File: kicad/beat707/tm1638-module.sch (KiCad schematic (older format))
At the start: 103 parts, among them SW10 SW_Push, SW11 SW_Push, SW12 SW_Push, SW13 SW_Push, SW14 SW_Push, SW15 SW_Push, SW16 SW_Push, SW17 SW_Push, SW18 SW_Push, SW19 SW_Push, SW20 SW_Push, SW21 SW_Push, SW22 SW_Push, SW23 SW_Push, SW24 SW_Push, SW25 SW_Push, SW26 SW_Push, SW27 SW_Push, SW28 SW_Push, SW5 SW_Push, SW6 SW_Push, SW7 SW_Push, SW8 SW_Push, SW9 SW_Push, U6 TM1638, U7 CA56-12EWA, U8 CA56-12EWA

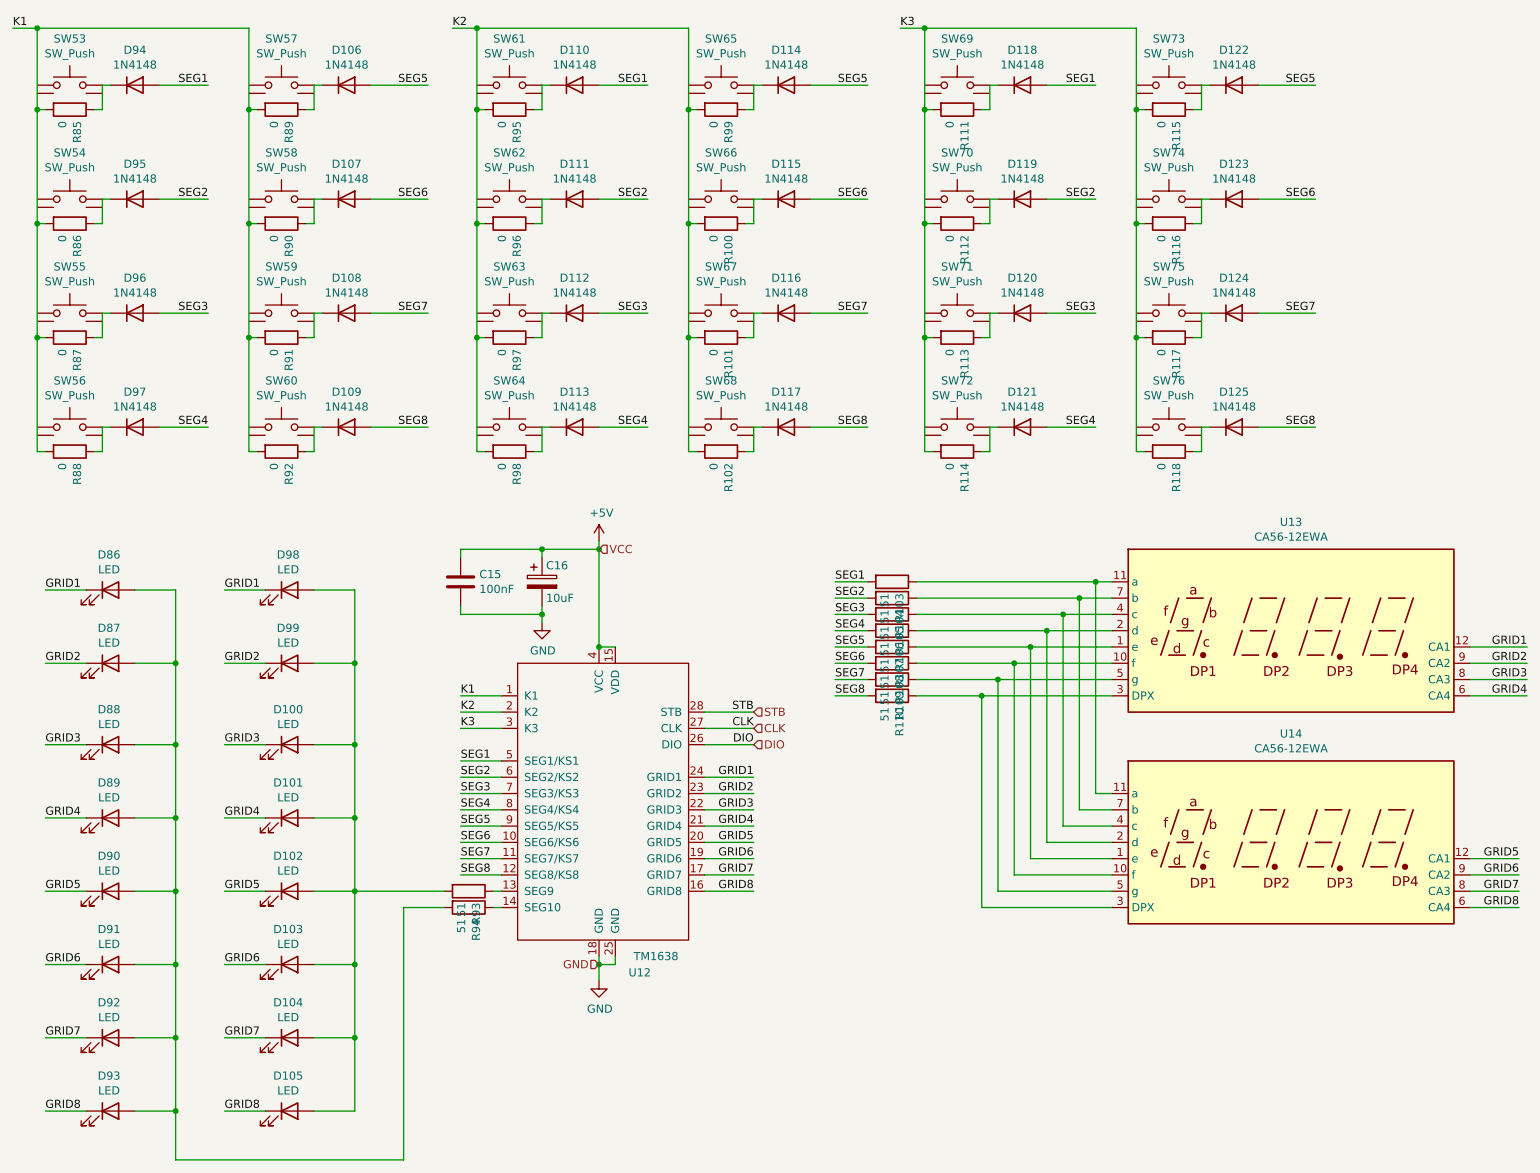
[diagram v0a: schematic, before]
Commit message: brain board added, bufixes and final board synchronized with schematic
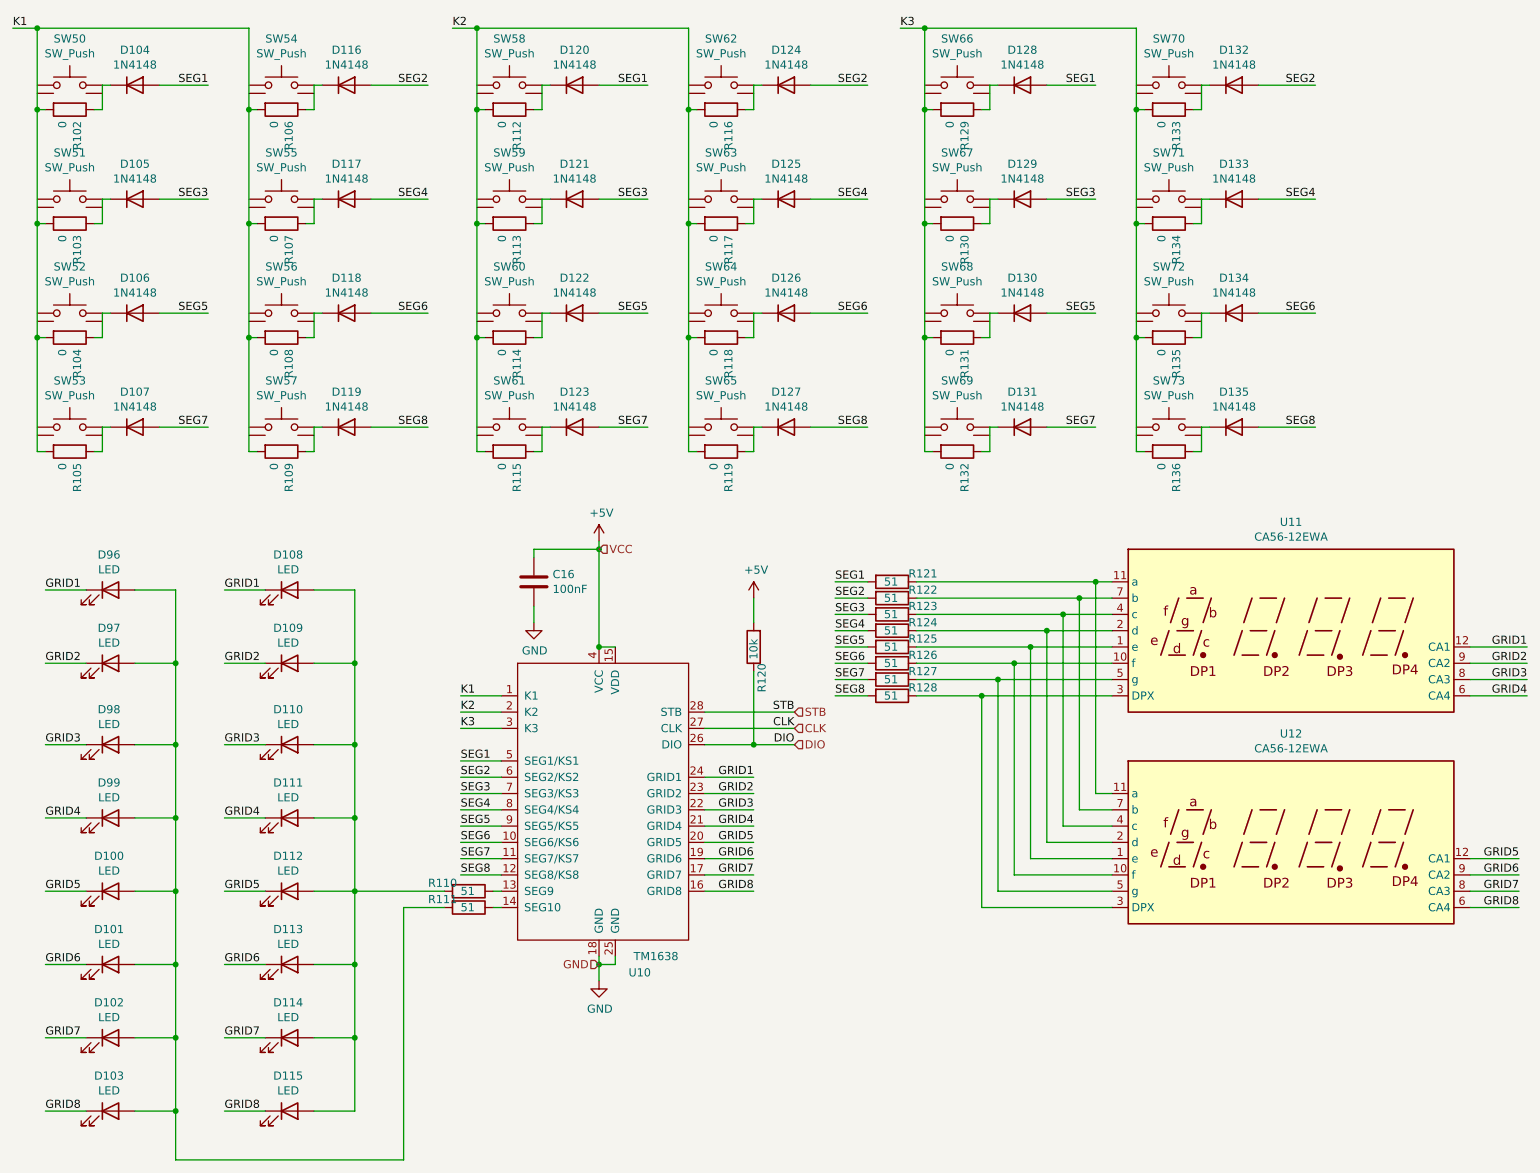
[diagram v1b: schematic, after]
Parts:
- removed C12: 10uF, Capacitor_THT:CP_Radial_D6.3mm_P2.50mm, symbol Device:CP
- added R85: 10k, Resistor_THT:R_Axial_DIN0207_L6.3mm_D2.5mm_P10.16mm_Horizontal, symbol Device:R
- R100: renamed from R83; footprint Resistor_THT:R_Axial_DIN0207_L6.3mm_D2.5mm_P7.62mm_Horizontal -> Resistor_THT:R_Axial_DIN0207_L6.3mm_D2.5mm_P10.16mm_Horizontal
- R101: renamed from R84; footprint Resistor_THT:R_Axial_DIN0207_L6.3mm_D2.5mm_P7.62mm_Horizontal -> Resistor_THT:R_Axial_DIN0207_L6.3mm_D2.5mm_P10.16mm_Horizontal
- R67: renamed from R51; footprint Resistor_THT:R_Axial_DIN0207_L6.3mm_D2.5mm_P7.62mm_Horizontal -> Resistor_THT:R_Axial_DIN0207_L6.3mm_D2.5mm_P10.16mm_Horizontal
- R68: renamed from R52; footprint Resistor_THT:R_Axial_DIN0207_L6.3mm_D2.5mm_P7.62mm_Horizontal -> Resistor_THT:R_Axial_DIN0207_L6.3mm_D2.5mm_P10.16mm_Horizontal
- R69: renamed from R53; footprint Resistor_THT:R_Axial_DIN0207_L6.3mm_D2.5mm_P7.62mm_Horizontal -> Resistor_THT:R_Axial_DIN0207_L6.3mm_D2.5mm_P10.16mm_Horizontal
- R70: renamed from R54; footprint Resistor_THT:R_Axial_DIN0207_L6.3mm_D2.5mm_P7.62mm_Horizontal -> Resistor_THT:R_Axial_DIN0207_L6.3mm_D2.5mm_P10.16mm_Horizontal
- R71: renamed from R55; footprint Resistor_THT:R_Axial_DIN0207_L6.3mm_D2.5mm_P7.62mm_Horizontal -> Resistor_THT:R_Axial_DIN0207_L6.3mm_D2.5mm_P10.16mm_Horizontal
- R72: renamed from R56; footprint Resistor_THT:R_Axial_DIN0207_L6.3mm_D2.5mm_P7.62mm_Horizontal -> Resistor_THT:R_Axial_DIN0207_L6.3mm_D2.5mm_P10.16mm_Horizontal
- R73: renamed from R57; footprint Resistor_THT:R_Axial_DIN0207_L6.3mm_D2.5mm_P7.62mm_Horizontal -> Resistor_THT:R_Axial_DIN0207_L6.3mm_D2.5mm_P10.16mm_Horizontal
- R74: renamed from R58; footprint Resistor_THT:R_Axial_DIN0207_L6.3mm_D2.5mm_P7.62mm_Horizontal -> Resistor_THT:R_Axial_DIN0207_L6.3mm_D2.5mm_P10.16mm_Horizontal
- R75: renamed from R59; footprint Resistor_THT:R_Axial_DIN0207_L6.3mm_D2.5mm_P7.62mm_Horizontal -> Resistor_THT:R_Axial_DIN0207_L6.3mm_D2.5mm_P10.16mm_Horizontal
- R76: renamed from R60; footprint Resistor_THT:R_Axial_DIN0207_L6.3mm_D2.5mm_P7.62mm_Horizontal -> Resistor_THT:R_Axial_DIN0207_L6.3mm_D2.5mm_P10.16mm_Horizontal
- R77: renamed from R61; footprint Resistor_THT:R_Axial_DIN0207_L6.3mm_D2.5mm_P7.62mm_Horizontal -> Resistor_THT:R_Axial_DIN0207_L6.3mm_D2.5mm_P10.16mm_Horizontal
- R78: renamed from R62; footprint Resistor_THT:R_Axial_DIN0207_L6.3mm_D2.5mm_P7.62mm_Horizontal -> Resistor_THT:R_Axial_DIN0207_L6.3mm_D2.5mm_P10.16mm_Horizontal
- R79: renamed from R63; footprint Resistor_THT:R_Axial_DIN0207_L6.3mm_D2.5mm_P7.62mm_Horizontal -> Resistor_THT:R_Axial_DIN0207_L6.3mm_D2.5mm_P10.16mm_Horizontal
- R80: renamed from R64; footprint Resistor_THT:R_Axial_DIN0207_L6.3mm_D2.5mm_P7.62mm_Horizontal -> Resistor_THT:R_Axial_DIN0207_L6.3mm_D2.5mm_P10.16mm_Horizontal
- R81: renamed from R65; footprint Resistor_THT:R_Axial_DIN0207_L6.3mm_D2.5mm_P7.62mm_Horizontal -> Resistor_THT:R_Axial_DIN0207_L6.3mm_D2.5mm_P10.16mm_Horizontal
- R82: renamed from R66; footprint Resistor_THT:R_Axial_DIN0207_L6.3mm_D2.5mm_P7.62mm_Horizontal -> Resistor_THT:R_Axial_DIN0207_L6.3mm_D2.5mm_P10.16mm_Horizontal
- R83: renamed from R67; footprint Resistor_THT:R_Axial_DIN0207_L6.3mm_D2.5mm_P7.62mm_Horizontal -> Resistor_THT:R_Axial_DIN0207_L6.3mm_D2.5mm_P10.16mm_Horizontal
- R84: renamed from R68; footprint Resistor_THT:R_Axial_DIN0207_L6.3mm_D2.5mm_P7.62mm_Horizontal -> Resistor_THT:R_Axial_DIN0207_L6.3mm_D2.5mm_P10.16mm_Horizontal
- R86: renamed from R69; footprint Resistor_THT:R_Axial_DIN0207_L6.3mm_D2.5mm_P7.62mm_Horizontal -> Resistor_THT:R_Axial_DIN0207_L6.3mm_D2.5mm_P10.16mm_Horizontal
- R87: renamed from R70; footprint Resistor_THT:R_Axial_DIN0207_L6.3mm_D2.5mm_P7.62mm_Horizontal -> Resistor_THT:R_Axial_DIN0207_L6.3mm_D2.5mm_P10.16mm_Horizontal
- R88: renamed from R71; footprint Resistor_THT:R_Axial_DIN0207_L6.3mm_D2.5mm_P7.62mm_Horizontal -> Resistor_THT:R_Axial_DIN0207_L6.3mm_D2.5mm_P10.16mm_Horizontal
- R89: renamed from R72; footprint Resistor_THT:R_Axial_DIN0207_L6.3mm_D2.5mm_P7.62mm_Horizontal -> Resistor_THT:R_Axial_DIN0207_L6.3mm_D2.5mm_P10.16mm_Horizontal
- R90: renamed from R73; footprint Resistor_THT:R_Axial_DIN0207_L6.3mm_D2.5mm_P7.62mm_Horizontal -> Resistor_THT:R_Axial_DIN0207_L6.3mm_D2.5mm_P10.16mm_Horizontal
- R91: renamed from R74; footprint Resistor_THT:R_Axial_DIN0207_L6.3mm_D2.5mm_P7.62mm_Horizontal -> Resistor_THT:R_Axial_DIN0207_L6.3mm_D2.5mm_P10.16mm_Horizontal
- R92: renamed from R75; footprint Resistor_THT:R_Axial_DIN0207_L6.3mm_D2.5mm_P7.62mm_Horizontal -> Resistor_THT:R_Axial_DIN0207_L6.3mm_D2.5mm_P10.16mm_Horizontal
- R93: renamed from R76; footprint Resistor_THT:R_Axial_DIN0207_L6.3mm_D2.5mm_P7.62mm_Horizontal -> Resistor_THT:R_Axial_DIN0207_L6.3mm_D2.5mm_P10.16mm_Horizontal
- R94: renamed from R77; footprint Resistor_THT:R_Axial_DIN0207_L6.3mm_D2.5mm_P7.62mm_Horizontal -> Resistor_THT:R_Axial_DIN0207_L6.3mm_D2.5mm_P10.16mm_Horizontal
- R95: renamed from R78; footprint Resistor_THT:R_Axial_DIN0207_L6.3mm_D2.5mm_P7.62mm_Horizontal -> Resistor_THT:R_Axial_DIN0207_L6.3mm_D2.5mm_P10.16mm_Horizontal
- R96: renamed from R79; footprint Resistor_THT:R_Axial_DIN0207_L6.3mm_D2.5mm_P7.62mm_Horizontal -> Resistor_THT:R_Axial_DIN0207_L6.3mm_D2.5mm_P10.16mm_Horizontal
- R97: renamed from R80; footprint Resistor_THT:R_Axial_DIN0207_L6.3mm_D2.5mm_P7.62mm_Horizontal -> Resistor_THT:R_Axial_DIN0207_L6.3mm_D2.5mm_P10.16mm_Horizontal
- R98: renamed from R81; footprint Resistor_THT:R_Axial_DIN0207_L6.3mm_D2.5mm_P7.62mm_Horizontal -> Resistor_THT:R_Axial_DIN0207_L6.3mm_D2.5mm_P10.16mm_Horizontal
- R99: renamed from R82; footprint Resistor_THT:R_Axial_DIN0207_L6.3mm_D2.5mm_P7.62mm_Horizontal -> Resistor_THT:R_Axial_DIN0207_L6.3mm_D2.5mm_P10.16mm_Horizontal
- renumbered C11 to C14, D6 to D16, D7 to D17, D8 to D18, D9 to D19, D10 to D20, D11 to D21, D12 to D22, D13 to D23, D18 to D28, D19 to D29, D20 to D30, D21 to D31, D22 to D32, D23 to D33, D24 to D34, D25 to D35, D54 to D64, D55 to D65, D56 to D66, D57 to D67, D66 to D76, D67 to D77, D68 to D78, D69 to D79, D70 to D80, D71 to D81, D72 to D82, D73 to D83, D74 to D84, D75 to D85, D76 to D86, D77 to D87, D78 to D88, D79 to D89, D80 to D90, D81 to D91, D82 to D92, D83 to D93, D84 to D94, D85 to D95, SW13 to SW10, SW14 to SW11, SW15 to SW12, SW16 to SW13, SW17 to SW14, SW18 to SW15, SW19 to SW16, SW20 to SW17, SW21 to SW18, SW22 to SW19, SW5 to SW2, SW23 to SW20, SW24 to SW21, SW25 to SW22, SW26 to SW23, SW27 to SW24, SW28 to SW25, SW6 to SW3, SW7 to SW4, SW8 to SW5, SW9 to SW6, SW10 to SW7, SW11 to SW8, SW12 to SW9, U6 to U4, U7 to U5, U8 to U6
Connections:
- net +5V: now also R85.2
- net DIO: now also R85.1
- net SEG2: now also D76.2 (A), D84.2 (A), D92.2 (A); no longer D65.2 (A), D81.2 (A), D89.2 (A)
- net SEG3: now also D65.2 (A), D81.2 (A), D89.2 (A); no longer D66.2 (A), D82.2 (A), D90.2 (A)
- net SEG4: now also D77.2 (A), D85.2 (A), D93.2 (A); no longer D67.2 (A), D83.2 (A), D91.2 (A)
- net SEG5: now also D66.2 (A), D82.2 (A), D90.2 (A); no longer D76.2 (A), D84.2 (A), D92.2 (A)
- net SEG6: now also D78.2 (A), D86.2 (A), D94.2 (A); no longer D77.2 (A), D85.2 (A), D93.2 (A)
- net SEG7: now also D67.2 (A), D83.2 (A), D91.2 (A); no longer D78.2 (A), D86.2 (A), D94.2 (A)
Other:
- moved on the sheet: C16

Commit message: mounting holes
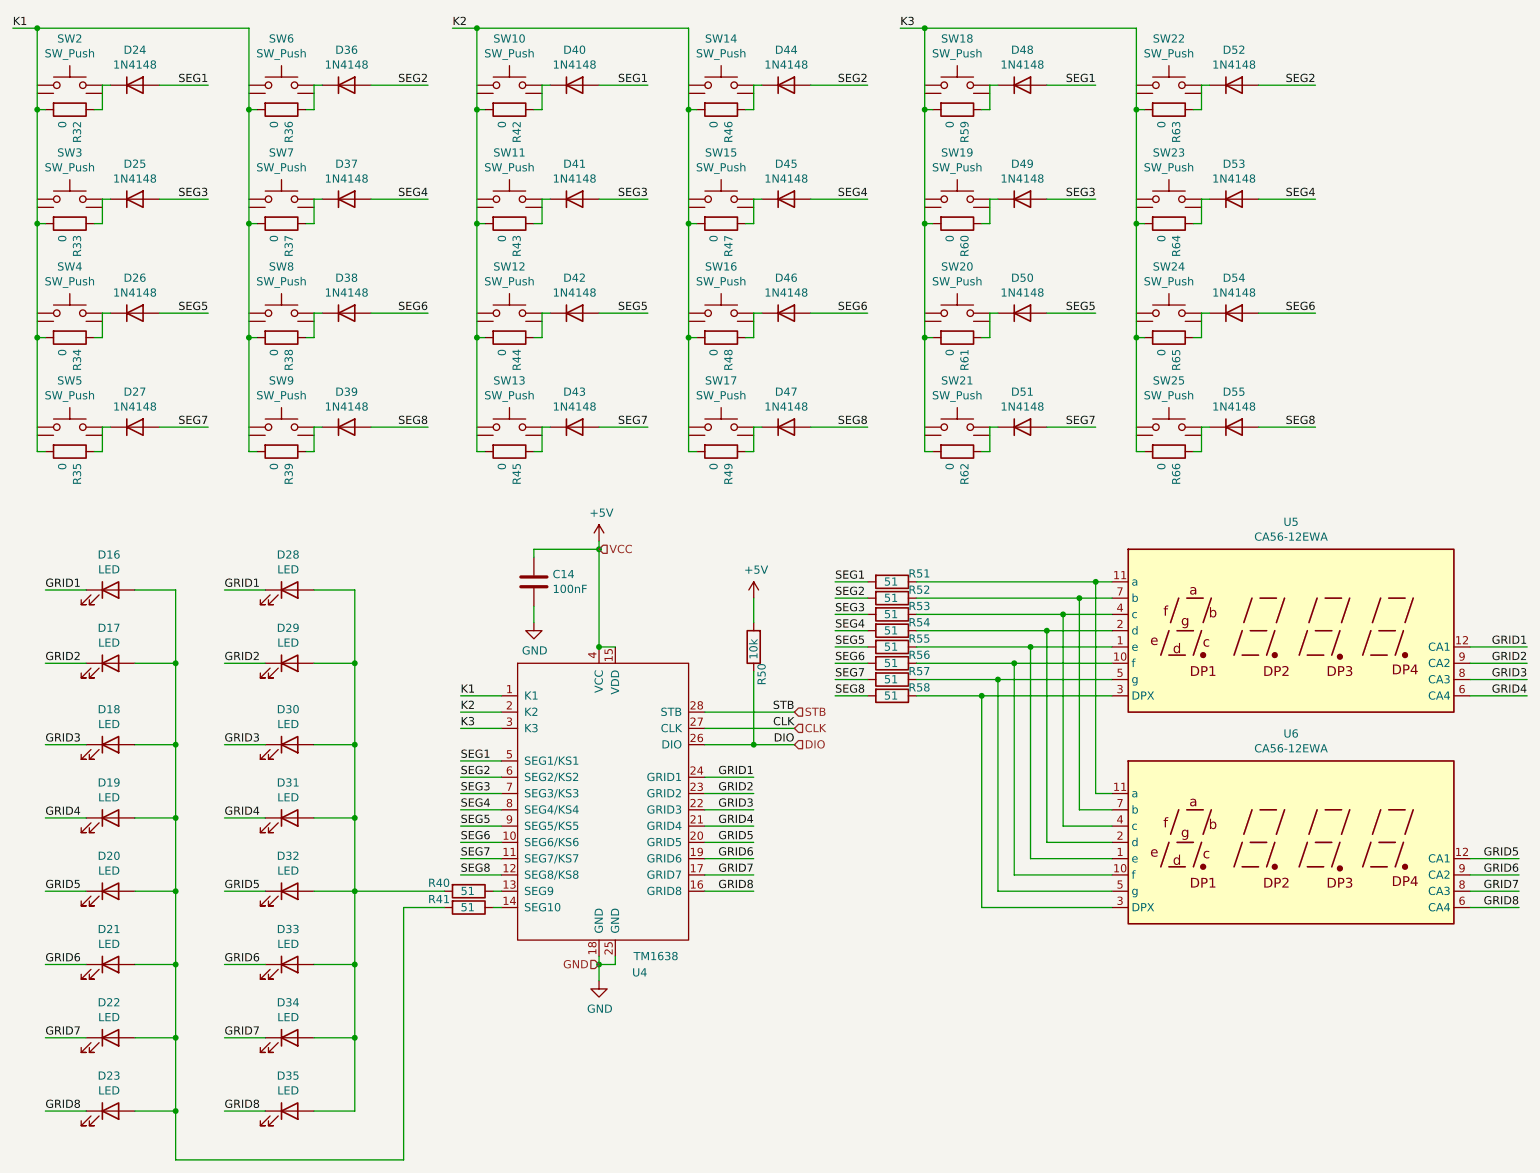
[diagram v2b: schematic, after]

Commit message: final component placement and routing
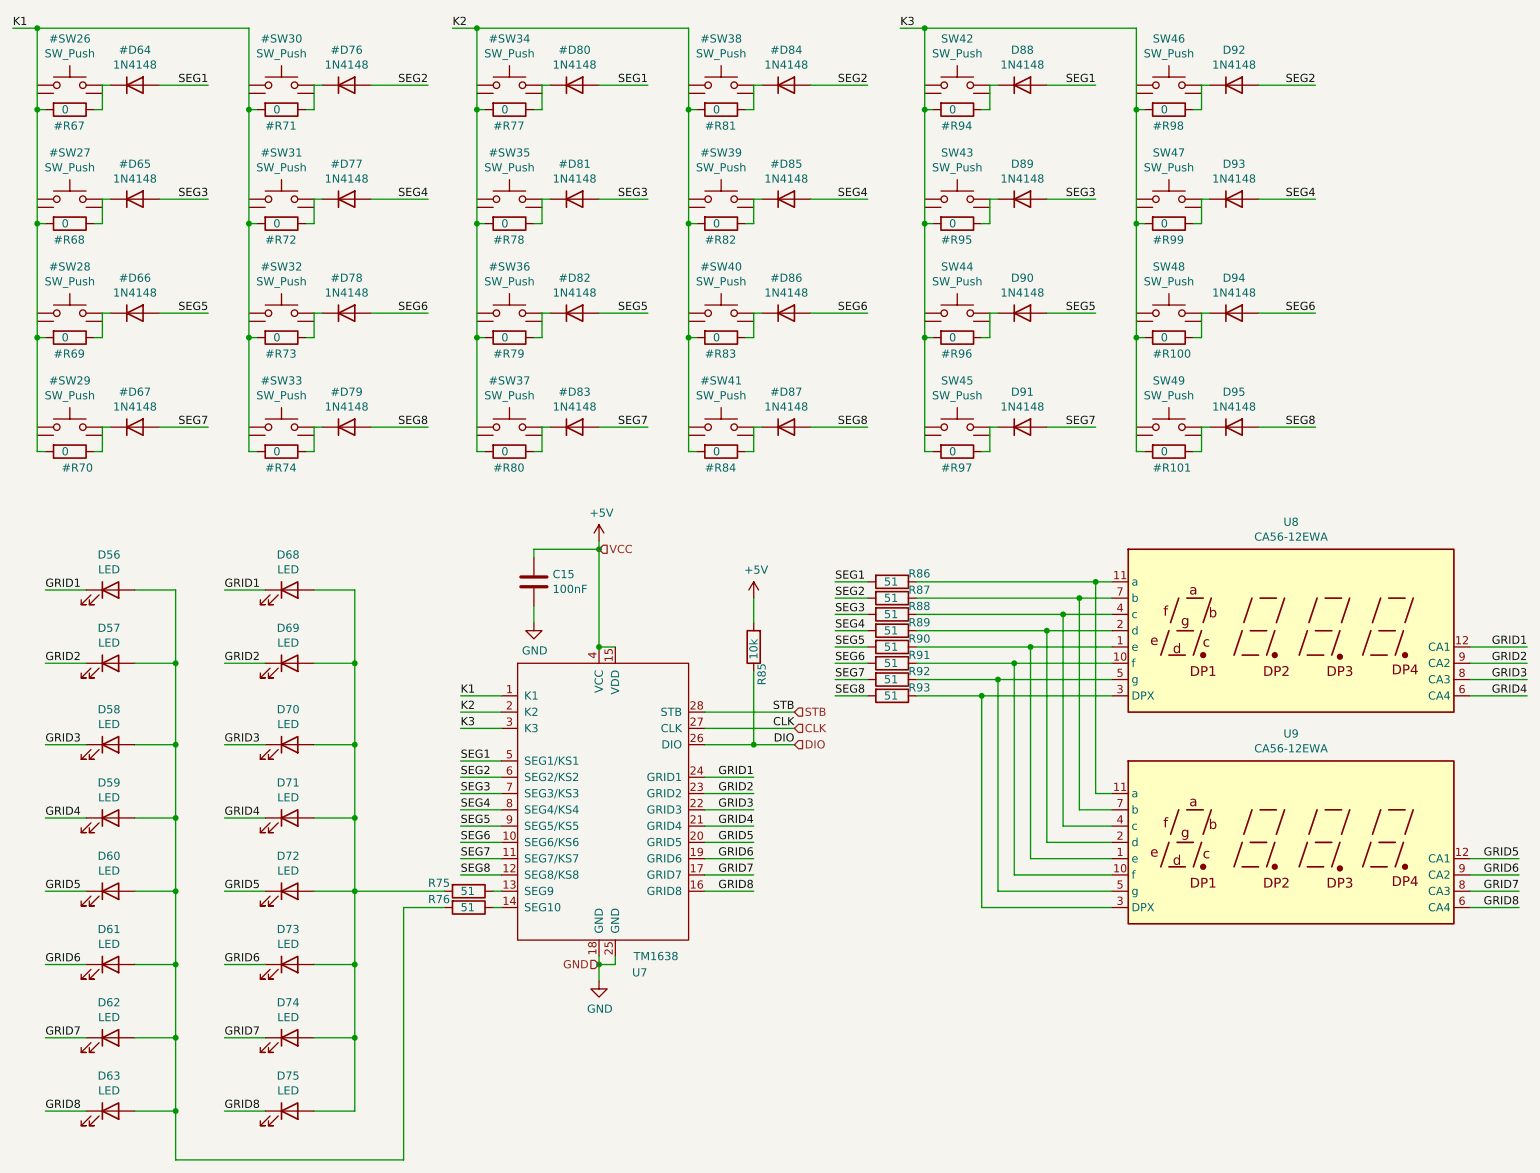
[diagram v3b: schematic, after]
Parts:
- removed D16, D17, D18, D19, D20, D21, D22, D23, D28, D29, D30, D31: LED, LED_THT:LED_D3.0mm, symbol Device:LED
- removed D64, D65, D66, D67, D76, D77, D78, D79, D80, D81, D82, D83, D84, D85, D86, D87: 1N4148, Diode_THT:D_DO-35_SOD27_P7.62mm_Horizontal, symbol Diode:1N4148
- removed R100, R101, R67, R68, R69, R70, R71, R72, R73, R74, R77, R78, R79, R80, R81, R82, R83, R84, R94, R95, R96, R97, R98, R99: 0, Resistor_THT:R_Axial_DIN0207_L6.3mm_D2.5mm_P10.16mm_Horizontal, symbol Device:R
- removed SW10, SW11, SW12, SW13, SW14, SW15, SW16, SW17, SW2, SW3, SW4, SW5, SW6, SW7, SW8, SW9: SW_Push, beat707:B3F-through-hole, symbol switch:SW_Push

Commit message: final routed version
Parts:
- R75, R76: value 51 -> 220
- R86, R87, R88, R89, R90, R91, R92, R93: value 51 -> 10
